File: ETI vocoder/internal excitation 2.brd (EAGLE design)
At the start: 160 x 100 mm, 49 parts, among them IC1 LM1458N, IC3 TL081P, IC4 UA741P, IC5 4006N, IC6 4030N, IC7 LM1458N, Q1 BC182L

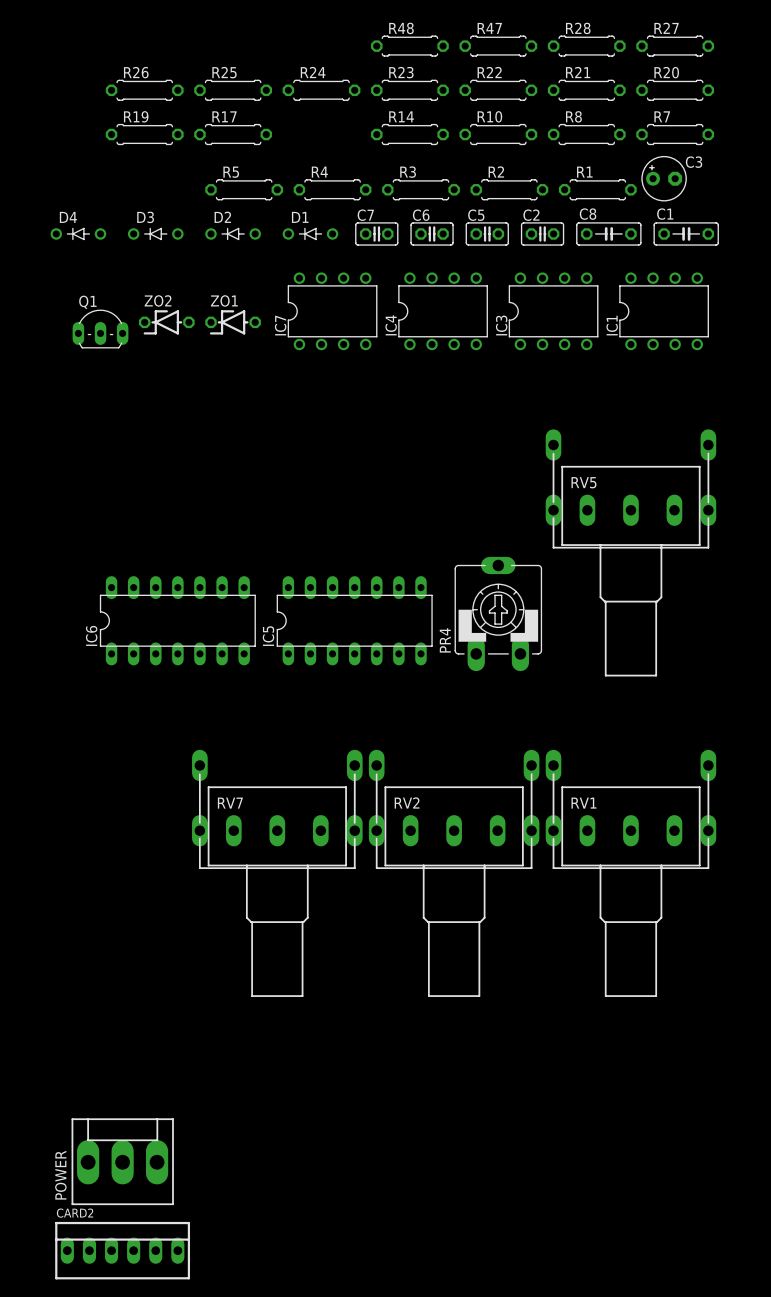
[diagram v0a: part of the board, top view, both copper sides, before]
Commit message: Internal excitation schematics
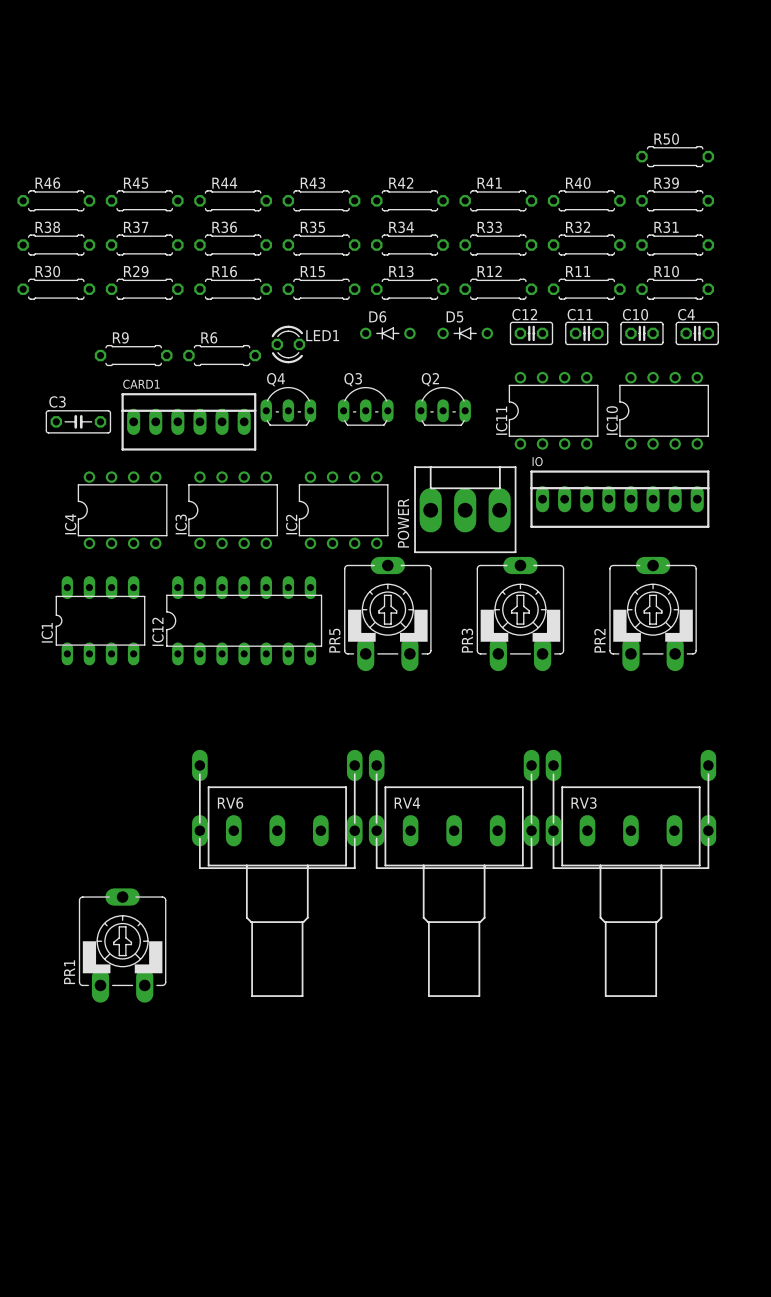
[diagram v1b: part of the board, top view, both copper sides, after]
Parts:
- removed C1: 100n, resistor:C050-025X075
- removed C2, C6: 100n, resistor:C025-025X050
- removed C5: 220p, resistor:C025-025X050
- removed C7: 100p, resistor:C025-025X050
- removed C8: 10n, resistor:C050-025X075
- removed CARD2: (no value), con-molex:22-23-2061
- removed D1, D2, D3, D4: 1N4148, joakim:DO35-5J
- removed IC5: 4006N, 40xx:DIL14
- removed IC6: 4030N, 40xx:DIL14
- removed IC7: LM1458N, linear:DIL08
- removed PR4: 2k2, pot:CA9V
- removed Q1: BC182L, transistor:TO92-ECB
- removed R1: 10k, resistor:0207/7
- removed R14: 1M, resistor:0207/7
- removed R17: 100k, resistor:0207/7
- removed R19: 15k, resistor:0207/7
- removed R2: 5k6, resistor:0207/7
- removed R20, R24, R25, R26, R27, R28: 4k7, resistor:0207/7
- removed R21: 22k, resistor:0207/7
- removed R22: 330k, resistor:0207/7
- removed R23: 27k, resistor:0207/7
- removed R3: 18k, resistor:0207/7
- removed R4: 560R, resistor:0207/7
- removed R47, R48: 1k, resistor:0207/7
- removed R5: 11k, resistor:0207/7
- removed R7: 150k, resistor:0207/7
- removed R8: 47k, resistor:0207/7
- removed RV5: 10k, joakim:POT16_W_BRACKET
- removed ZO1, ZO2: 5V1, diode:ZDIO-5
- added C10, C4: 100n, resistor:C025-025X050
- added C11: 22n, resistor:C025-025X050
- added C12: 1u0, resistor:C025-025X050
- added CARD1: (no value), con-molex:22-23-2061
- added D5, D6: 1N4148, joakim:DO35-5J
- added IC10, IC11, IC2: LM1458N, linear:DIL08
- added IC12: 4016N, 40xx:DIL14
- added IO: 22-23-2081, con-molex:22-23-2081
- added LED1: (no value), led:LED3MM
- added PR1, PR2: 100k, pot:CA9V
- added PR3: 220k, pot:CA9V
- added PR5: 2k2, pot:CA9V
- added Q2, Q4: BC212L, transistor:TO92-CBE
- added Q3: BC182L, transistor:TO92-ECB
- added R11: 18k, resistor:0207/7
- added R12: 560R, resistor:0207/7
- added R13: 11k, resistor:0207/7
- added R15: 150k, resistor:0207/7
- added R16, R35, R39, R43, R6: 47k, resistor:0207/7
- added R29, R34, R40, R44, R45, R50, R9: 10k, resistor:0207/7
- added R30, R42: 1M, resistor:0207/7
- added R31: 3k9, resistor:0207/7
- added R32: 22k, resistor:0207/7
- added R33, R38: 470k, resistor:0207/7
- added R36, R37, R46: 1k5, resistor:0207/7
- added R41: 1k, resistor:0207/7
- C3: value (none) -> 100n; device resistor:E2,5-5 -> resistor:C050-025X075
- IC1: value LM1458N -> CA3080E; device linear:DIL08 -> synthdiy:DIL08
- IC4: value UA741P -> TL082P
- R10: value 1k -> 5k6
- moved POWER 84.6 mm to (-41.9, 57.1)
- moved IC1 73.9 mm to (-83.8, 44.5)
- moved C3 72.9 mm to (-86.4, 67.3)
- moved IC3 43.3 mm to (-68.6, 57.1)
- moved IC4 43.3 mm to (-81.3, 57.1)
- moved R10 27.0 mm to (-17.8, 82.5)
- renumbered RV1 to RV3, RV2 to RV4, RV7 to RV6
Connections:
- removed net 1_12: IC5.1, IC5.12
- removed net 4_10: IC5.10, IC5.4, IC6.8
- removed net 5_9: IC5.5, IC5.9, IC6.13
- removed net N$32: C5.1, C7.1, IC5.3, IC6.4
- new net 2KHZ: C12.1, IC10.6, IO.8, R40.1
- new net 4KHZ: C11.1, IC10.2, IO.7, R39.1
- new net EXT_EXCIT: IO.4, R6.2
- new net N$34: IC11.5, PR3.S
- new net N$35: IC11.6, IC11.7, IC12.1
- new net N$37: D5.A, IC4.7, R32.2
- new net N$38: IC4.1, IC4.2, IC4.5
- new net N$41: D5.C, IC4.6, R31.1
- new net N$42: C10.2, IC4.3, R29.2, R30.1
- new net OUT: IO.5, IO.6
- new net OUTPUT: IC12.2, IC12.3
- new net V_UV_ON_OFF: IO.2, IO.3, R50.1
- net +12V: now also IC10.8, IC11.8, IC2.8, IC4.8, IO.1, PR1.A, PR2.E, R13.1; no longer IC1.8, IC4.7, IC7.8, R10.2, R14.2, R5.1, ZO1.C
- net -12V: now also IC10.4, IC11.4, IC2.4, PR1.E, PR2.A; no longer IC1.4, IC7.4, ZO2.A
- net BOARD2_MIX: now also CARD1.4, R16.1, R6.1; no longer CARD2.4
- net GND: now also C10.1, IC10.3, IC10.5, IC12.12, IC12.6, IC2.2, IC2.5, PR3.A, Q2.B, R12.2, R30.2, R31.2, R36.2, R37.2, RV6.1A; no longer C3.-, C6.2, C7.2, IC1.2, IC1.5, IC4.3, IC7.3, Q1.E, R4.2, R47.1, R48.2, RV5.1A, RV6.1E
- net N$1: now also IC2.3, R10.1, R9.1; no longer IC1.3, R1.1, R2.1
- net N$10: now also R15.2; no longer R7.2
- net N$11: now also C4.2, R15.1; no longer C2.2, R7.1
- net N$12: now also C4.1; no longer C2.1
- net N$13: now also R16.2; no longer R8.2
- net N$14: now also IC11.3, R41.2, R42.1; no longer IC4.2, R17.2, R8.1, RV6.1S
- net N$15: now also C11.2, IC10.1, IC11.2, R39.2; no longer D1.A, D2.C, IC7.1
- net N$16: now also IC11.1, R42.2, R43.1; no longer IC7.2, R14.1, R24.1, R25.2, R26.2
- net N$17: now also C12.2, IC10.7, R40.2, R41.1; no longer D1.C, IC7.5, R26.1
- net N$18: now also LED1.A, R46.2; no longer D2.A, R25.1, R27.2
- net N$19: now also IC12.5, Q3.C, R44.1, R45.2; no longer IC7.6, R27.1, R28.2
- net N$2: now also IC2.1, R9.2; no longer IC1.1, R1.2
- net N$20: now also Q4.B, R45.1; no longer D3.C, R28.1
- net N$21: now also D6.C, Q3.B, R43.2, R50.2; no longer D3.A, D4.A, IC7.7
- net N$23: now also IC12.13, Q4.C, R46.1; no longer IC6.3, IC6.5, R23.1
- net N$25: now also IC1.3, R35.1, R36.1; no longer C8.1, R19.2
- net N$26: now also IC1.2, R37.1, R38.1; no longer C8.2, IC5.6, IC6.10
- net N$27: now also PR2.S, R38.2; no longer IC6.9, Q1.C, R20.1
- net N$28: now also IC1.5, R34.2; no longer IC6.11, R21.1
- net N$29: now also Q2.E, R34.1; no longer IC6.2, R22.1
- net N$3: now also R11.2; no longer R3.2
- net N$30: now also Q2.C, R32.1, R33.2; no longer C5.2, R22.2, R23.2
- net N$31: now also PR1.S, R33.1; no longer IC5.13, IC6.12
- net N$33: now also IC1.6, PR3.E; no longer Q1.B, R21.2
- net N$4: now also C3.1, IC2.6, R11.1; no longer C1.1, IC1.6, R3.1
- net N$5: now also R12.1; no longer R4.1
- net N$6: now also C3.2, IC2.7, R10.2; no longer C1.2, IC1.7, R2.2
- net N$7: now also RV6.1S; no longer RV5.1S
- net N$8: now also PR5.A, R13.2; no longer PR4.A, R5.2
- net N$9: now also PR5.E, PR5.S, RV6.1E; no longer PR4.E, PR4.S, RV5.1E
- net VCA_CTRL: now also CARD1.2, R29.1; no longer CARD2.2, D4.C
- net VCA_SIGNAL: now also CARD1.1, R35.2; no longer C6.1, CARD2.1, R19.1, RV6.1A
- net VDD: now also CARD1.5, IC12.14, Q4.E, R44.2; no longer C3.+, CARD2.5, IC5.14, IC6.1, IC6.14, IC6.6, R10.1, R20.2, R47.2, ZO1.A
- net VSS: now also CARD1.6, D6.A, IC12.7, LED1.K, Q3.E; no longer CARD2.6, IC5.7, IC6.7, R48.1, ZO2.C
- net X: now also CARD1.3, IC12.4; no longer CARD2.3, IC4.6, R17.1, R24.2

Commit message: All ETI boards checked for caps and pots
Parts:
- removed CARD1: (no value), con-molex:22-23-2061
- removed IC1: CA3080E, synthdiy:DIL08
- removed IC4: TL082P, linear:DIL08
- added BOARD2: 22-23-2041, con-molex:22-23-2041
- added BOARD2-PWR: 22-23-2021, con-molex:22-23-2021
- added IC8: TL082P, linear:DIL08
- added IC9: CA3080E, joakim:DIL08
- C10: device resistor:C025-025X050 -> resistor:C075-032X103
- C11, C12: device resistor:C025-025X050 -> resistor:C050-025X075
- C3: device resistor:C050-025X075 -> resistor:C075-032X103
- R6: device resistor:0207/7 -> resistor:0207/10
- moved R38 177.1 mm to (72.4, 14.6), turned to 180 degrees
- moved R16 171.2 mm to (91.4, 21.6), turned to 270 degrees
- moved R37 169.3 mm to (72.4, 11.4), turned to 180 degrees
- moved R46 163.7 mm to (65.4, 38.1), turned to 270 degrees
- moved R36 161.8 mm to (72.4, 8.26), turned to 180 degrees
- moved R35 160.9 mm to (88.3, 21.6), turned to 90 degrees
- moved R6 157.9 mm to (85.1, 44.5), turned to 180 degrees
- moved R30 148.9 mm to (41.9, 11.4), turned to 180 degrees
- moved IC12 147.5 mm to (80.0, 38.1)
- moved R45 146.5 mm to (57.1, 38.1), turned to 270 degrees
- moved R34 144.7 mm to (83.8, 28.6)
- moved LED1 137.6 mm to (68.6, 33.7), turned to 270 degrees
- moved PR1 134.7 mm to (52.7, 21.6), turned to 270 degrees
- moved R44 134.2 mm to (54.0, 38.1), turned to 90 degrees
- moved R15 131.0 mm to (54.0, 15.2), turned to 180 degrees
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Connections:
- removed net N$33: IC1.6, PR3.E
- removed net OUTPUT: IC12.2, IC12.3
- new net N$22: IC9.6, PR3.A
- net +12V: now also IC8.8, IC9.7, IO.5, PR2.A; no longer IC4.8, IO.1, PR2.E
- net -12V: now also IC8.4, IC9.4, PR2.E; no longer IC4.4, PR2.A
- net 2KHZ: now also IO.1; no longer IO.8
- net 4KHZ: now also IO.2; no longer IO.7
- net BOARD2_MIX: now also BOARD2.4; no longer CARD1.4
- net EXT_EXCIT: now also IO.8; no longer IO.4
- net GND: now also PR3.E, RV6.1E; no longer PR3.A, RV6.1A
- net N$25: now also IC9.3; no longer IC1.3
- net N$26: now also IC9.2; no longer IC1.2
- net N$28: now also IC9.5; no longer IC1.5
- net N$37: now also IC8.7; no longer IC4.7
- net N$38: now also IC8.1, IC8.2, IC8.5; no longer IC4.1, IC4.2, IC4.5
- net N$41: now also IC8.6; no longer IC4.6
- net N$42: now also IC8.3; no longer IC4.3
- net N$9: now also RV6.1A; no longer RV6.1E
- net OUT: now also IC12.2, IC12.3, IO.7; no longer IO.5
- net VCA_CTRL: now also BOARD2.2; no longer CARD1.2
- net VCA_SIGNAL: now also BOARD2.3; no longer CARD1.1
- net VDD: now also BOARD2-PWR.2; no longer CARD1.5
- net VSS: now also BOARD2-PWR.1; no longer CARD1.6
- net V_UV_ON_OFF: now also IO.4; no longer IO.2
- net X: now also BOARD2.1; no longer CARD1.3
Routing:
- net GND: track 0.00 -> 248.2 mm
- net -12V: track 0.00 -> 158.8 mm
- net +12V: track 0.00 -> 150.7 mm
- net VCA_CTRL: track 0.00 -> 71.1 mm
- net VSS: track 0.00 -> 61.2 mm
- net N$35: track 0.00 -> 60.6 mm
- net OUT: track 0.00 -> 53.1 mm
- net N$22: track 0.00 -> 47.8 mm
- net N$10: track 0.00 -> 46.8 mm
- net EXT_EXCIT: track 0.00 -> 43.8 mm
- net 4KHZ: track 0.00 -> 42.7 mm
- net N$19: track 0.00 -> 37.7 mm
- net N$9: track 0.00 -> 33.2 mm
- net N$6: track 0.00 -> 32.8 mm
- net VDD: track 0.00 -> 32.3 mm
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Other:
- board size 160 x 100 mm -> 94 x 53.6 mm
- board text added: "+12V"
- board text added: "+7C"
- board text added: "-12V"
- board text added: "-7V"
- board text added: "12V"
- board text added: "4V&B"
- board text added: "<2kHz"
- board text added: ">4kHz"
- board text added: "ETI Vocoder"
- board text added: "Ext exc"
- board text added: "GND"
- board text added: "Internal Excitation"
- board text added: "Lower board v1.0"
- board text added: "MIX"
- board text added: "Output"
- board text added: "PR4"
- board text added: "V/UV"
- board text added: "VCA ctrl"
- board text added: "VCA sig"
- board text added: "X"

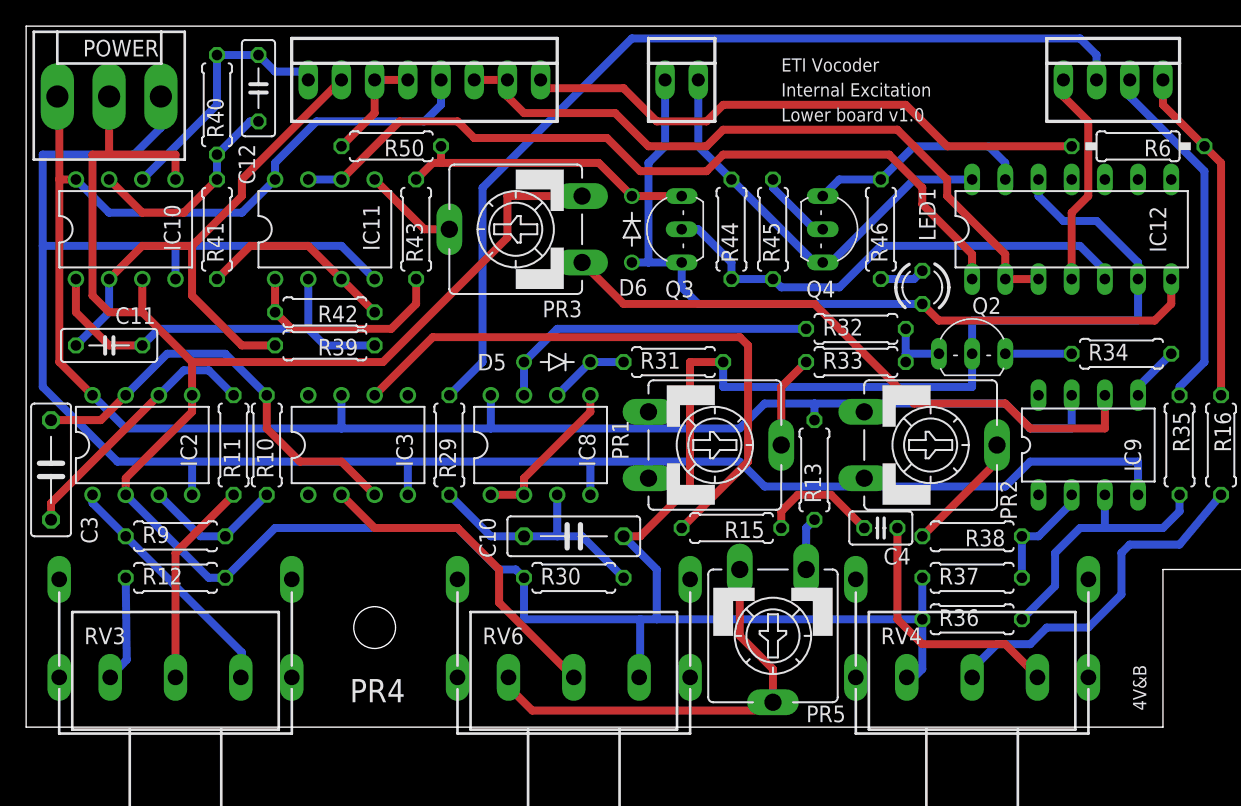
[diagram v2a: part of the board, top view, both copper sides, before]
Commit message: Fixed input boards in regards to article and added spacer holes
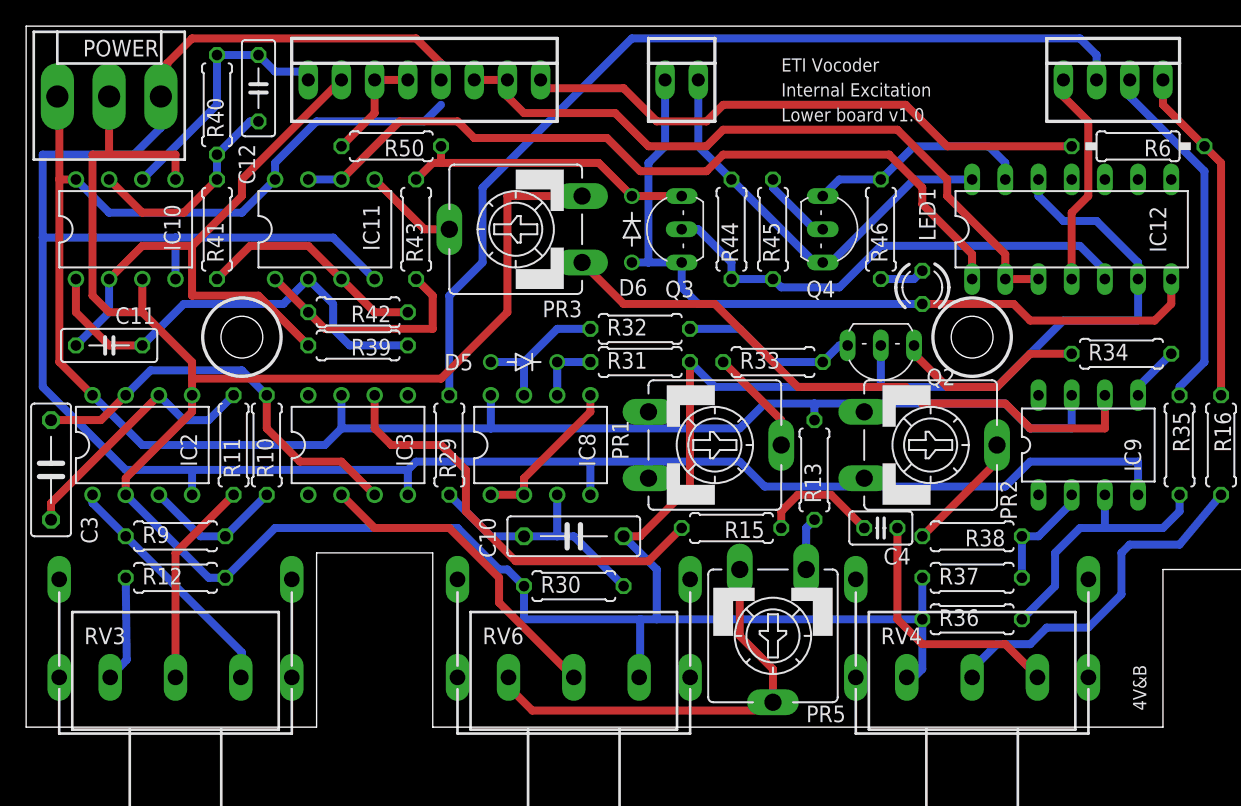
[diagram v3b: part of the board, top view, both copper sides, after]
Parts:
- C4: value 100n -> 10n
- moved R32 16.5 mm to (47.0, 30.5)
- moved Q2 7.01 mm to (65.4, 29.2), turned to 180 degrees
- moved R33 6.35 mm to (57.1, 27.9)
- moved D5 2.54 mm to (38.1, 27.9)
- moved R31 2.54 mm to (47.0, 27.9)
- moved R39 2.54 mm to (25.4, 29.2)
- moved R42 2.54 mm to (25.4, 31.8)
- moved R30 0.63 mm to (41.9, 10.8)
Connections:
- removed net N$29: Q2.E, R34.1
- new net N$24: Q2.C, R34.1
- net +12V: no longer IO.5
- net -12V: now also IO.5
- net N$30: now also Q2.E; no longer Q2.C
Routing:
- net -12V: track 158.8 -> 185.5 mm
- net N$24: track 0.00 -> 14.8 mm
- net N$37: track 25.2 -> 11.2 mm
- net N$10: track 46.8 -> 33.2 mm
- net N$30: track 5.08 -> 13.6 mm
- net N$29: track 5.08 -> 0.00 mm
- net N$15: track 31.3 -> 34.3 mm
- net GND: track 248.2 -> 250.8 mm
- net 4KHZ: track 42.7 -> 45.2 mm
- net N$14: track 15.2 -> 17.8 mm
- net N$16: track 16.6 -> 18.0 mm
- net N$6: track 32.8 -> 31.8 mm
- net N$41: track 6.13 -> 5.08 mm
- net N$31: track 7.14 -> 8.19 mm
- net +12V: track 150.7 -> 149.9 mm
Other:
- outline, holes or cut-outs redrawn
- board text removed: "PR4"

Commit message: Fixed wrong value for C11/C15 on internal excitation board (should be 220uF, not 22uF)
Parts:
- C11: value 22n -> 220n
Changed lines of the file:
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@@
 <attribute name="VALUE" x="64.8462" y="40.386" size="1.27" layer="27" ratio="10" rot="R270"/>
 </element>
-<element name="C11" library="resistor" package="C050-025X075" value="22n" x="6.35" y="29.21" smashed="yes">
+<element name="C11" library="resistor" package="C050-025X075" value="220n" x="6.35" y="29.21" smashed="yes">
 <attribute name="NAME" x="9.906" y="32.131" size="1.27" layer="25" ratio="10" rot="R180"/>
 <attribute name="VALUE" x="4.064" y="26.416" size="1.27" layer="27" ratio="10"/>
